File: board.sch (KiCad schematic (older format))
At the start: 50 parts, among them J1 LASER, J10 Mode, J11 Y, J12 12V, J13 Y, J14 X, J15 12V-36V, J16 CNC_OUT2, J2 Pololu_Breakout_A4988, J3 V_LASER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

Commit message: Organize schematic sheet
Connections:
- no-connect marks 0 -> 4
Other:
- moved on the sheet: C1, C2, C3, C4, C7, C8, C9, D2, D3, D5, J11, J12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

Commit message: Reduce ERC
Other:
- moved on the sheet: C1, C2, C3, D2, D5, J11, J13, J14, J2, J4, J5, J6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

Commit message: Merge main 12V networks
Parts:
- Q1: symbol Device:Q_NMOS_GDS -> Device:Q_PNP_BEC
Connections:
- net V_STEP_MOT is gone; now on net +12V: C1.1, C2.1, C3.1, D5.1 (K), J12.1 (Pin_1), J2.8 (VMOT), J4.8 (VMOT), J6.8 (VMOT), K1.2
- net V_LASER renamed +12V
- net relay.p5 renamed spindle_ctl
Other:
- note added: "Vout = 1.25 + ( 1 + R4 / R2 ) \nVout = 12.36 V"
- moved on the sheet: C2, C5, D1, D4, J1, J12, J15, J3, K1, Q2, R3, R5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

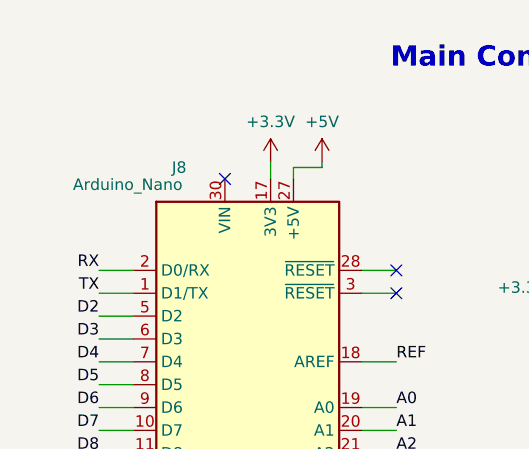
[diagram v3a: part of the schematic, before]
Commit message: Power on the Arduino
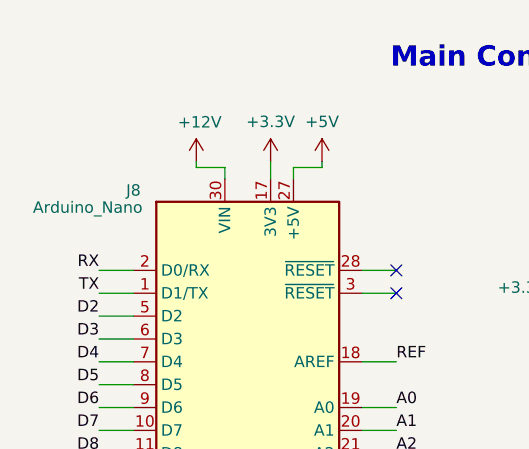
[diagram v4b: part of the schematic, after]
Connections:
- net +12V: now also J8.30 (VIN)
- no-connect marks 4 -> 3
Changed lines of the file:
@@
 Wire Wire Line
 	1625 3500 1625 3575
-$Comp
-L MCU_Module:Arduino_Nano_v3.x J8
-U 1 1 5E00F681
-P 1625 2500
-F 0 "J8" H 1325 3550 50  0000 C CNN
-F 1 "Arduino_Nano" H 1100 3475 50  0000 C CNN
-F 2 "Developower:Arduino_Nano" H 1625 2500 50  0001 C CIN
-F 3 "http://www.mouser.com/pdfdocs/Gravitech_Arduino_Nano3_0.pdf" H 1625 2500 50  0001 C CNN
-	1    1625 2500
-	1    0    0    -1
-$EndComp
 Text Label 3800 3550 0    50   ~ 0
 D11
@@
 NoConn ~ 2275 2000
 NoConn ~ 2275 1900
-NoConn ~ 1525 1500
 $Comp
 L power:PWR_FLAG #FLG0101
@@
 Wire Wire Line
 	4850 4575 4725 4575
+$Comp
+L power:+12V #PWR?
+U 1 1 6088AE8B
+P 1400 1425
+F 0 "#PWR?" H 1400 1275 50  0001 C CNN
+F 1 "+12V" H 1415 1598 50  0000 C CNN
+F 2 "" H 1400 1425 50  0001 C CNN
+F 3 "" H 1400 1425 50  0001 C CNN
+	1    1400 1425
+	1    0    0    -1
+$EndComp
+Wire Wire Line
+	1525 1500 1525 1450
+Wire Wire Line
+	1525 1450 1400 1450
+Wire Wire Line
+	1400 1425 1400 1450
+$Comp
+L MCU_Module:Arduino_Nano_v3.x J8
+U 1 1 5E00F681
+P 1625 2500
+F 0 "J8" H 1125 3450 50  0000 C CNN
+F 1 "Arduino_Nano" H 925 3375 50  0000 C CNN
+F 2 "Developower:Arduino_Nano" H 1625 2500 50  0001 C CIN
+F 3 "http://www.mouser.com/pdfdocs/Gravitech_Arduino_Nano3_0.pdf" H 1625 2500 50  0001 C CNN
+	1    1625 2500
+	1    0    0    -1
+$EndComp
 $EndSCHEMATC

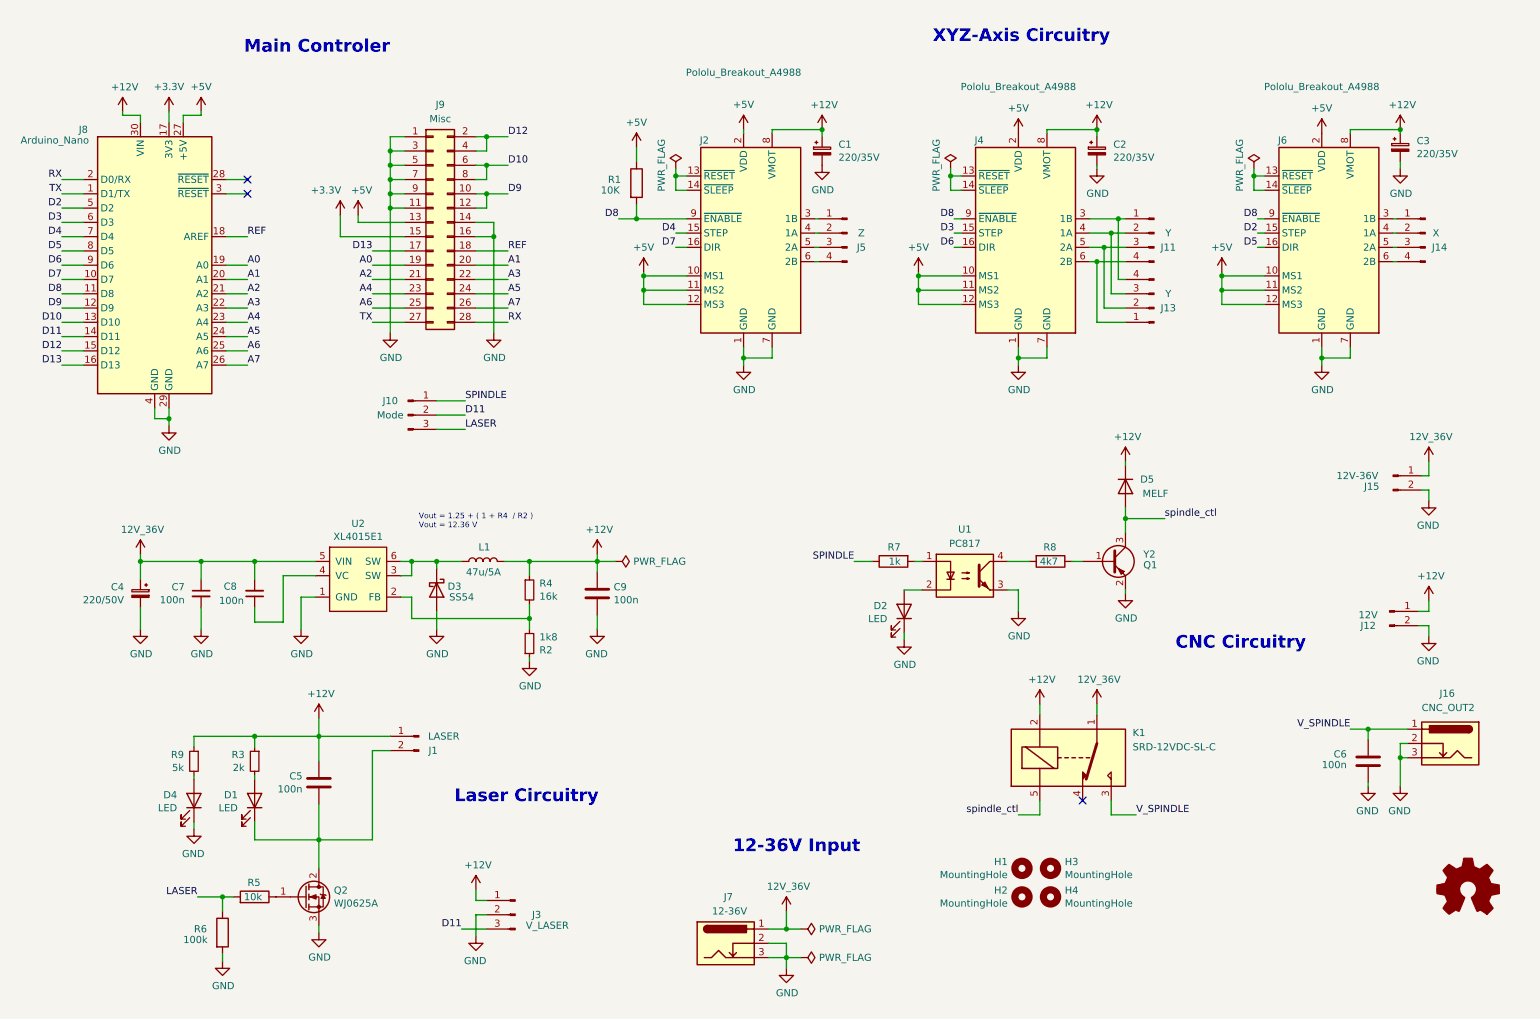
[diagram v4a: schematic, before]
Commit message: Update using Kicad 5.1.12
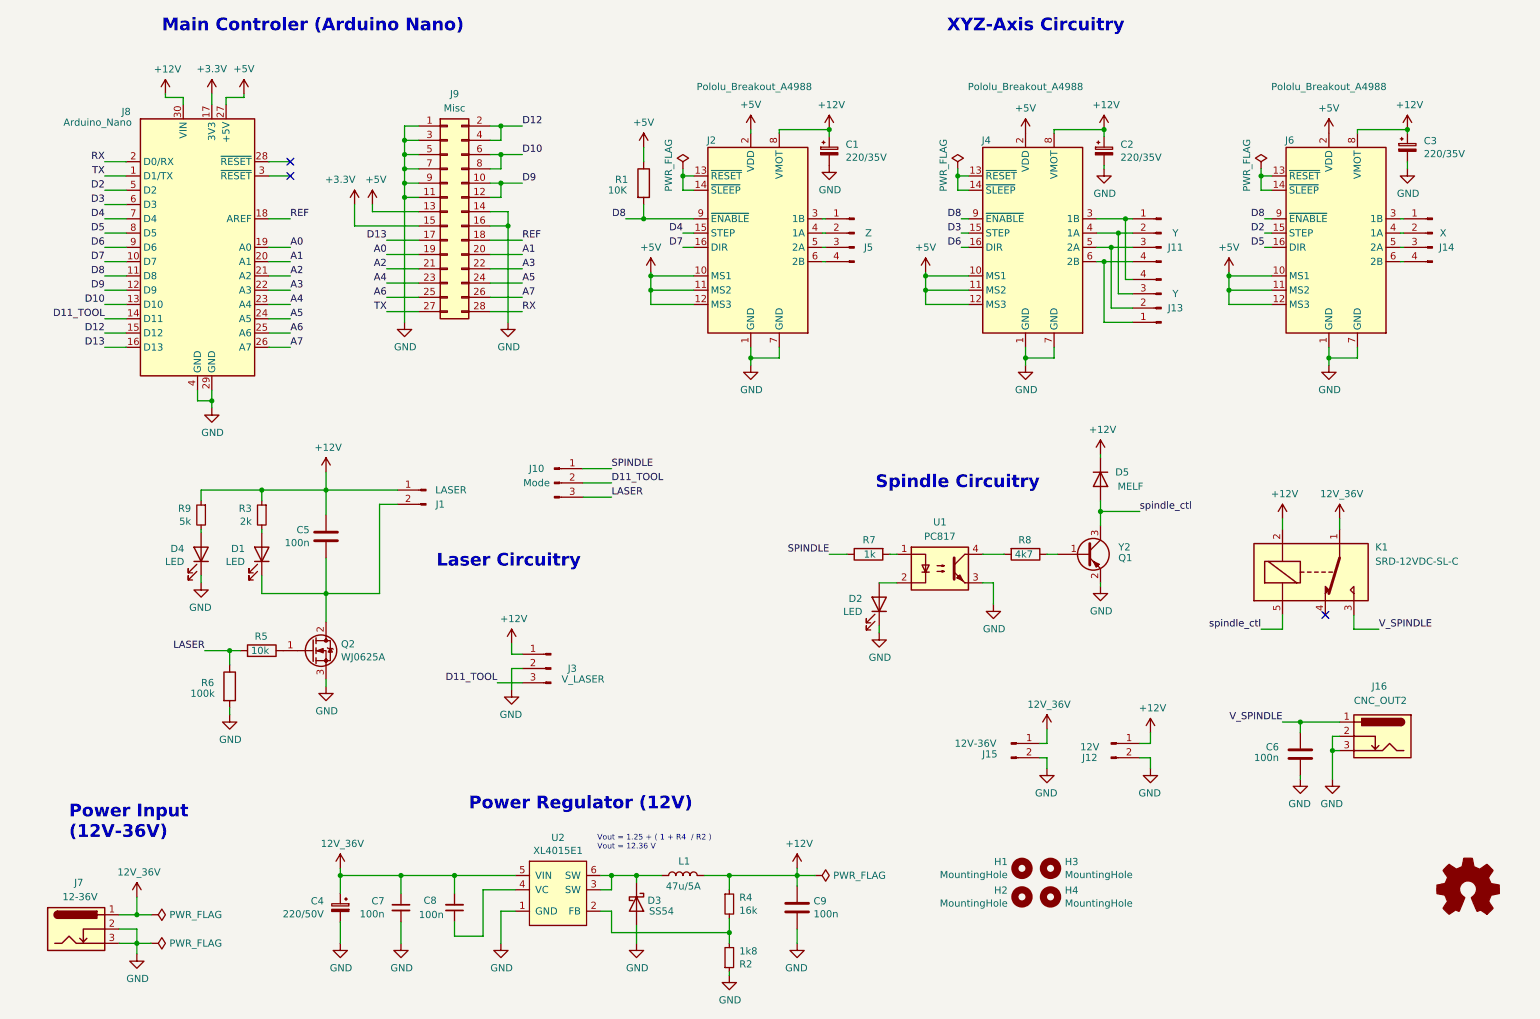
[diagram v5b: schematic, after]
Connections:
- net D11 renamed D11_TOOL
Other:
- note added: "Main Controler (Arduino Nano)"
- note added: "Power Input\n(12V-36V)"
- note added: "Power Regulator (12V)"
- note added: "Spindle Circuitry"
- note removed: "12-36V Input"
- note removed: "CNC Circuitry"
- note removed: "Main Controler"
- moved on the sheet: C1, C2, C3, C4, C5, C6, C7, C8, C9, D1, D2, D3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
